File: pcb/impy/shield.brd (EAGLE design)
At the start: 133 x 107 mm, 118 parts, among them J1 USB-2410-06, J2 SI-60062-F, J3 5V, U1 AD5933YRS, U10 LTC3406AB, U11 23LCV1024-I/SN, U12 MIC2009A-1YM6, U13 ADG725BSU, U14 ADG725BSU, U2 ADG704BRM, U3 AD8656ARZ, U4 M24C08WMN, U5 ADG706BRU, U6 DP83848I, U7 MIC2009A-1YM6, U8 AT25DF081A-SS, U9 SST25VF080B-80-4I-S2

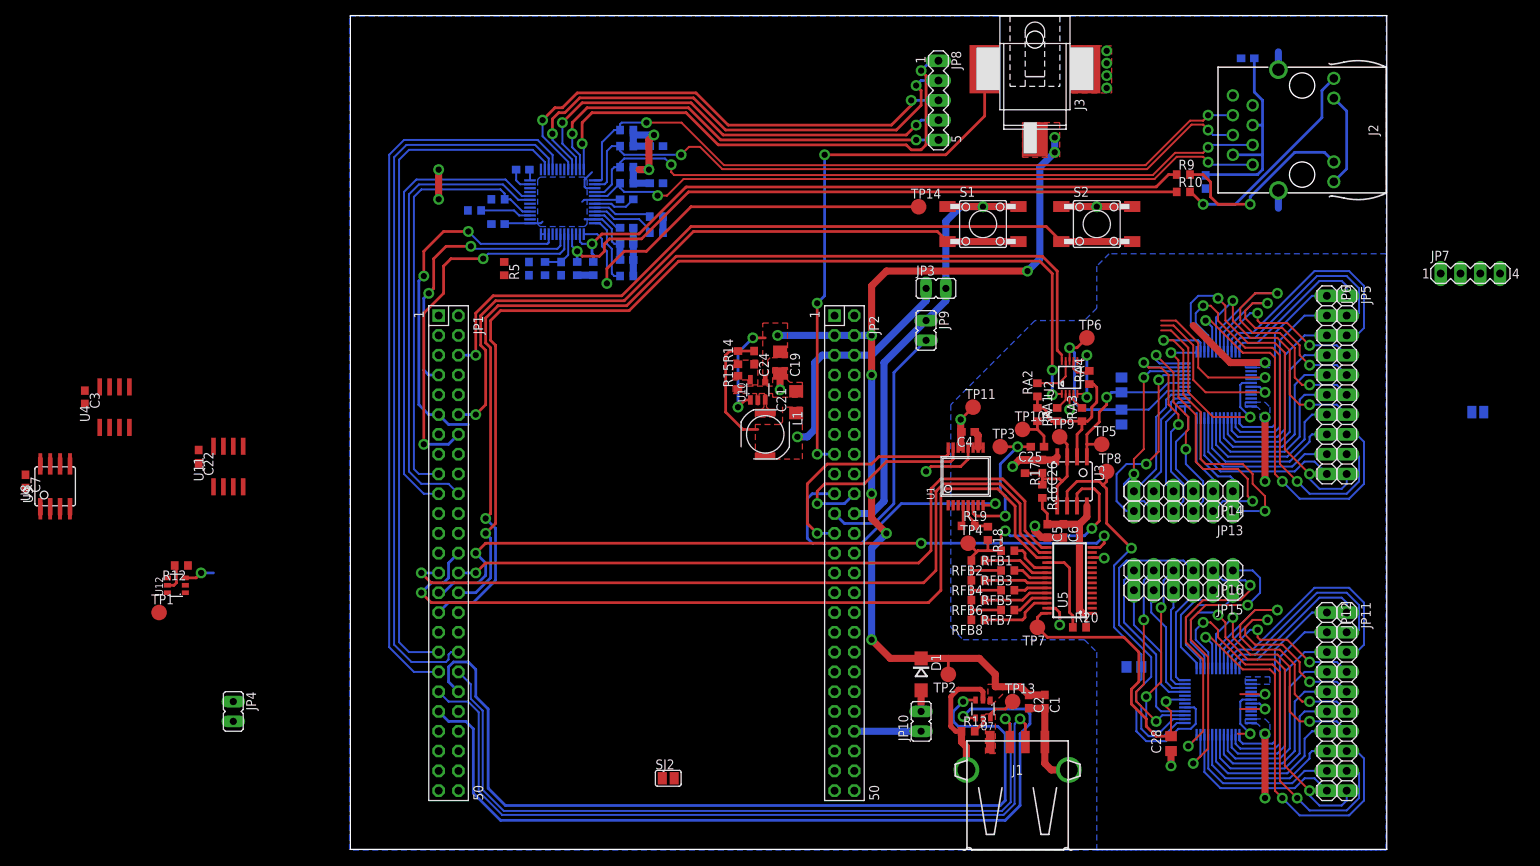
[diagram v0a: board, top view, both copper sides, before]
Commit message: * pcb/impy: (shield.brd) Layout analog circuits and power supply for those.
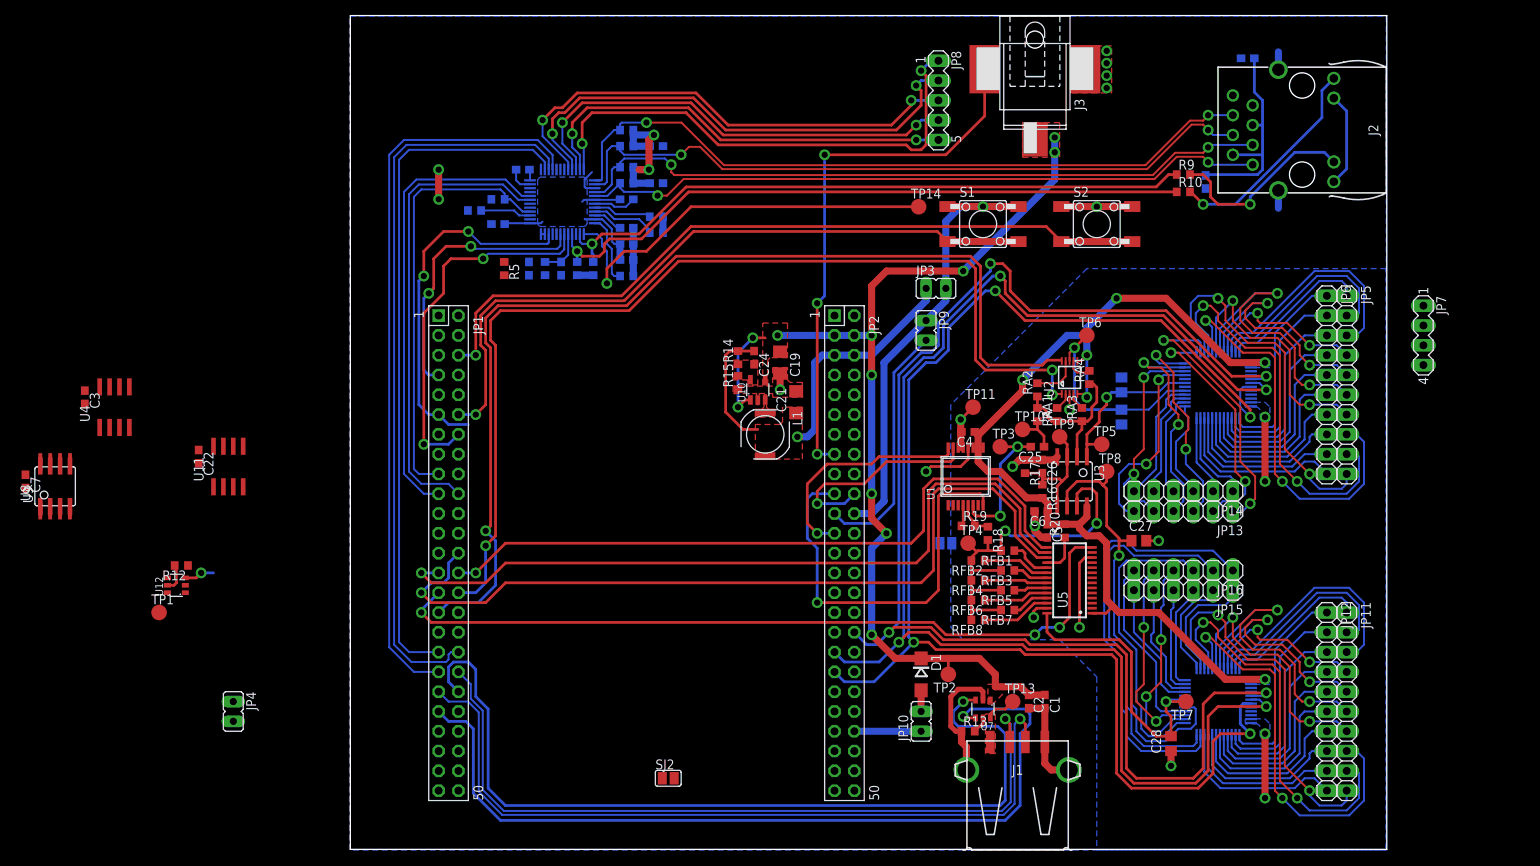
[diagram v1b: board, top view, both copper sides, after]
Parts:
- moved SJ1 70.3 mm to (38.4, 34.3)
- moved TP7 21.3 mm to (69.2, 14.0)
- moved C27 16.2 mm to (63.2, 34.6), flipped to the top
- moved R20 12.5 mm to (53.7, 35.9), turned to 90 degrees
- moved JP7 9.97 mm to (99.7, 61.0), turned to 270 degrees
- moved C6 3.82 mm to (50.6, 38.4), turned to 180 degrees
- moved TP6 0.32 mm to (56.5, 61.0)
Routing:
- net PD2: track 25.1 -> 180.9 mm, vias 2 -> 4
- net PC10: track 26.8 -> 180.1 mm, vias 2 -> 4
- net PC12: track 33.3 -> 181.7 mm, vias 2 -> 4
- net VCC: track 116.6 -> 193.7 mm, vias 5 -> 8
- net PB8: track 37.0 -> 53.0 mm
- net N$96: track 40.3 -> 55.8 mm, vias 2 -> 0
- net N$97: track 36.0 -> 49.8 mm, vias 2 -> 0
- net AGND: track 42.9 -> 52.2 mm, vias 11 -> 12
- net N$107: track 11.0 -> 5.15 mm
- net PE11: track 94.6 -> 100.2 mm
- net N$78: track 41.0 -> 35.5 mm
- net +5V: track 139.8 -> 134.6 mm
- net N$79: track 35.2 -> 31.2 mm
- net PE9: track 100.1 -> 98.3 mm
- net PE10: track 91.0 -> 89.2 mm
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
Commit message: * pcb/impy: (shield.sch) Fix supply of I2C header, should be VDD in case this is supplied from the discovery board or does not match VCC for some other reason.
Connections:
- net VCC: no longer JP7.4
- net VDD: now also JP7.4
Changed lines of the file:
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@@
 <wire x1="35.8775" y1="62.865" x2="30.48" y2="57.4675" width="0.9144" layer="16"/>
 <wire x1="30.48" y1="57.4675" x2="30.48" y2="39.6875" width="0.9144" layer="16"/>
+<contactref element="JP7" pad="4"/>
+<wire x1="47.73" y1="77.4975" x2="99.695" y2="57.15" width="0" layer="19" extent="1-1"/>
 <wire x1="-24.13" y1="60.96" x2="30.48" y2="57.4675" width="0" layer="19" extent="16-16"/>
 <wire x1="-26.67" y1="60.96" x2="-24.13" y2="60.96" width="0" layer="19" extent="1-1"/>
@@
 <contactref element="U11" pad="8"/>
 <contactref element="U11" pad="7"/>
-<contactref element="JP7" pad="4"/>
 <contactref element="J2" pad="2"/>
 <contactref element="J2" pad="5"/>
@@
 <wire x1="79.0575" y1="91.1225" x2="88.2015" y2="91.4019" width="0" layer="19" extent="16-16"/>
 <wire x1="66.675" y1="65.7225" x2="71.755" y2="81.495" width="0" layer="19" extent="1-16"/>
-<wire x1="99.695" y1="57.15" x2="79.375" y2="57.4675" width="0" layer="19" extent="1-1"/>
 <wire x1="2.12" y1="74.13625" x2="42.125" y2="48.5775" width="0" layer="19" extent="1-16"/>
 <wire x1="0.42" y1="80.48625" x2="2.12" y2="76.2" width="0" layer="19" extent="16-16"/>

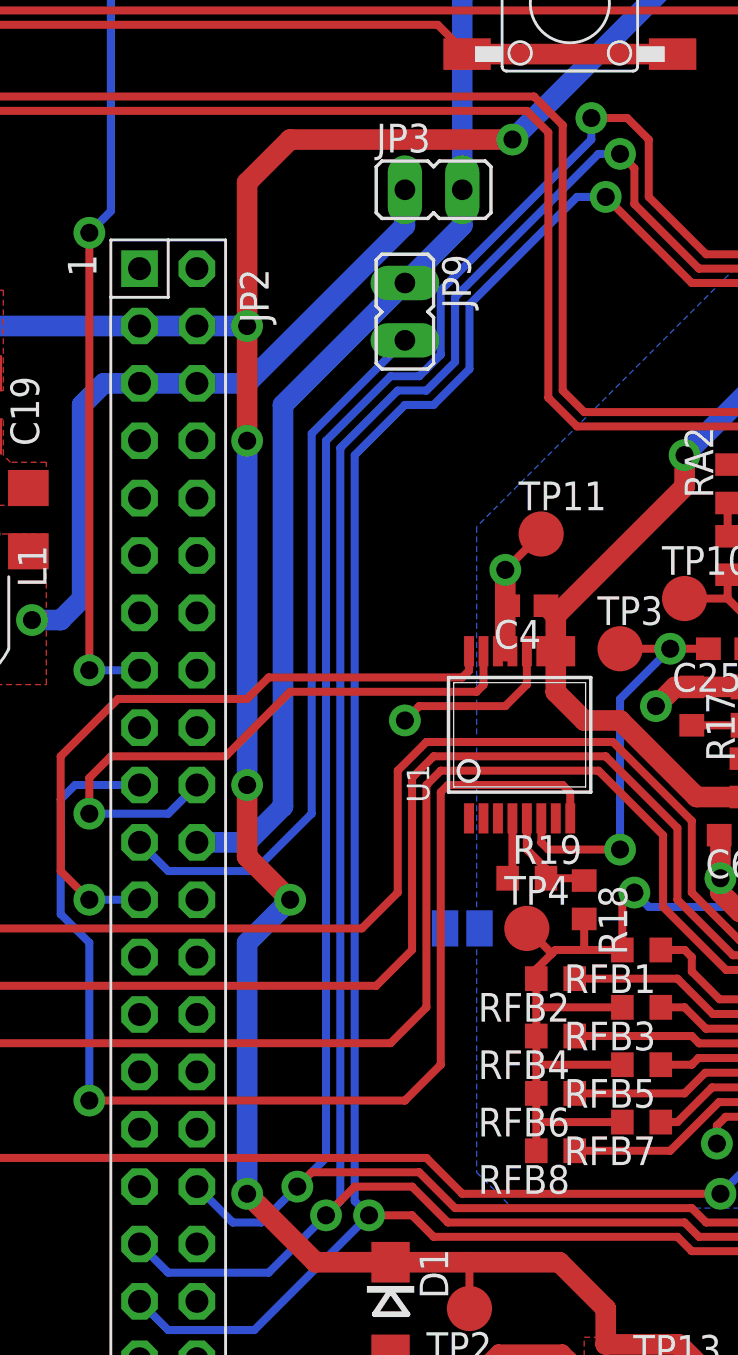
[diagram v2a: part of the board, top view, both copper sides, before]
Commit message: * pcb/impy: (shield.sch) Remove unnecessary BOOT0 jumper, this can be accessed on the discovery board directly.
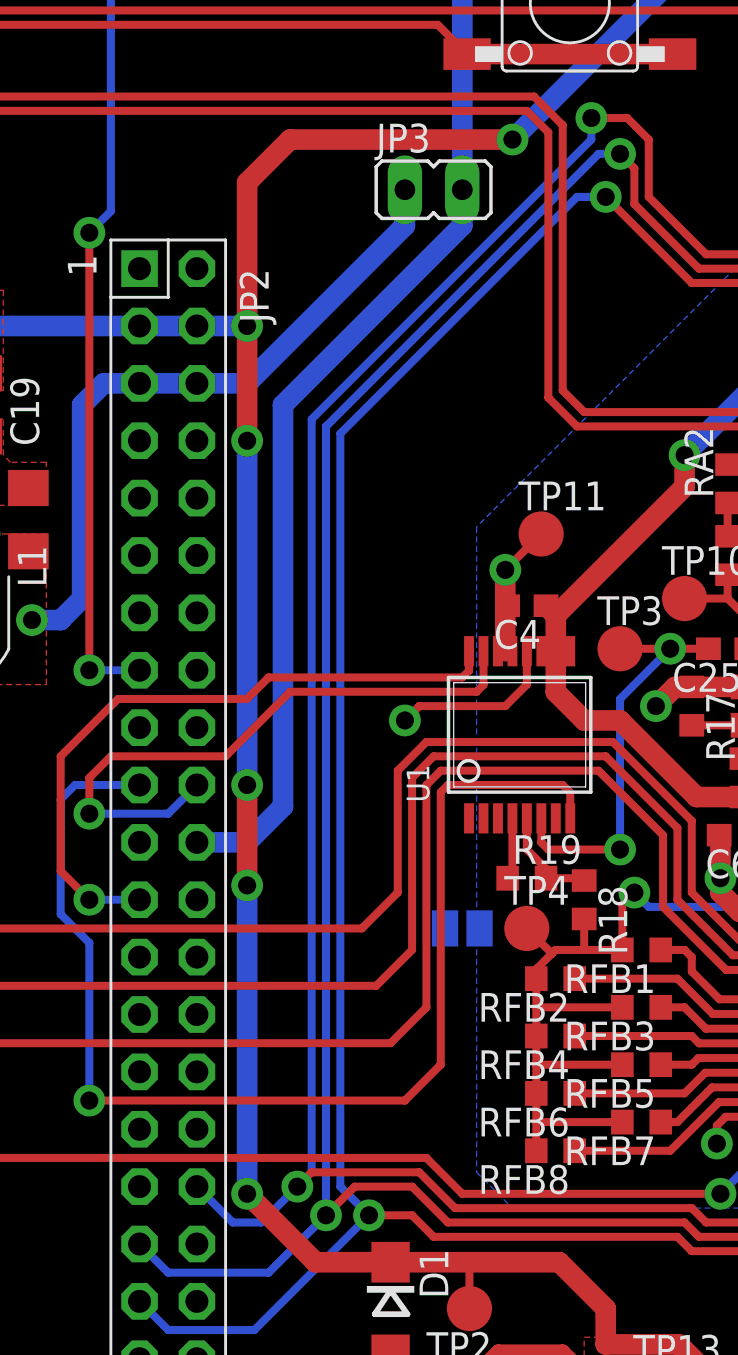
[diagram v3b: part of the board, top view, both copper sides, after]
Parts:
- removed JP9: BOOT0, jumper:JP1
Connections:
- net BOOT0: no longer JP9.2
- net VDD: no longer JP9.1
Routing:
- net BOOT0: track 31.9 -> 0.00 mm
- net +5V: track 134.6 -> 133.0 mm
- net PD2: track 180.9 -> 180.1 mm
- net PC12: track 181.7 -> 180.9 mm
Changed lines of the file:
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@@
 <element name="R11" library="rcl" package="R0603" value="2k2" x="-13.0175" y="69.5325" rot="MR270"/>
 <element name="SJ2" library="jumper" package="SJ" value="ETH_CLK" x="2.794" y="4.1275"/>
-<element name="JP9" library="jumper" package="JP1" value="BOOT0" x="35.8775" y="61.595" rot="R180"/>
 <element name="S2" library="parts" package="FSM" value="FSM4JSMATR" x="57.785" y="75.2475" rot="R270">
 <attribute name="RS" value="718-2455" x="28.575" y="56.1975" size="1.778" layer="27" rot="R270" display="off"/>
@@
 <contactref element="JP1" pad="3"/>
 <contactref element="JP2" pad="22"/>
-<contactref element="JP9" pad="1"/>
 <contactref element="S1" pad="4"/>
 <contactref element="S1" pad="3"/>
@@
 <wire x1="43.1525" y1="77.4975" x2="43.18" y2="77.47" width="0.9144" layer="16"/>
 <wire x1="38.4175" y1="66.9925" x2="38.4175" y2="65.405" width="0.9144" layer="16"/>
-<wire x1="38.4175" y1="65.405" x2="35.8775" y2="62.865" width="0.9144" layer="16"/>
-<wire x1="35.8775" y1="62.865" x2="30.48" y2="57.4675" width="0.9144" layer="16"/>
 <wire x1="30.48" y1="57.4675" x2="30.48" y2="39.6875" width="0.9144" layer="16"/>
 <contactref element="JP7" pad="4"/>
+<wire x1="30.48" y1="57.4675" x2="38.4175" y2="65.405" width="0.9144" layer="16"/>
 <wire x1="47.73" y1="77.4975" x2="99.695" y2="57.15" width="0" layer="19" extent="1-1"/>
 <wire x1="-24.13" y1="60.96" x2="30.48" y2="57.4675" width="0" layer="19" extent="16-16"/>
@@
 <wire x1="28.8925" y1="55.88" x2="28.8925" y2="40.64" width="0.9144" layer="16"/>
 <via x="28.8925" y="40.64" extent="1-16" drill="0.8" shape="octagon"/>
-<via x="30.7975" y="35.56" extent="1-16" drill="0.8" shape="octagon"/>
+<via x="28.8925" y="36.195" extent="1-16" drill="0.8" shape="octagon"/>
 <via x="28.8925" y="22.5425" extent="1-16" drill="0.8" shape="octagon"/>
 <wire x1="28.8925" y1="22.5425" x2="31.9225" y2="19.5125" width="0.9144" layer="1"/>
-<wire x1="28.8925" y1="40.64" x2="28.8925" y2="37.465" width="0.9144" layer="1"/>
-<wire x1="28.8925" y1="37.465" x2="30.7975" y2="35.56" width="0.9144" layer="1"/>
-<wire x1="30.7975" y1="35.56" x2="28.8925" y2="33.655" width="0.9144" layer="16"/>
-<wire x1="28.8925" y1="33.655" x2="28.8925" y2="22.5425" width="0.9144" layer="16"/>
+<wire x1="28.8925" y1="40.64" x2="28.8925" y2="36.195" width="0.9144" layer="1"/>
+<wire x1="28.8925" y1="36.195" x2="28.8925" y2="22.5425" width="0.9144" layer="16"/>
 <via x="40.64" y="69.215" extent="1-16" drill="0.8" shape="octagon"/>
 <wire x1="40.64" y1="69.215" x2="30.7975" y2="69.215" width="0.9144" layer="1"/>
@@
 <signal name="BOOT0">
 <contactref element="JP2" pad="21"/>
-<contactref element="JP9" pad="2"/>
-<wire x1="24.13" y1="38.1" x2="25.4" y2="36.83" width="0.3556" layer="16"/>
-<wire x1="25.4" y1="36.83" x2="29.21" y2="36.83" width="0.3556" layer="16"/>
-<wire x1="29.21" y1="36.83" x2="31.75" y2="39.37" width="0.3556" layer="16"/>
-<wire x1="31.75" y1="39.37" x2="31.75" y2="56.1975" width="0.3556" layer="16"/>
-<wire x1="31.75" y1="56.1975" x2="35.8775" y2="60.325" width="0.3556" layer="16"/>
 </signal>
 <signal name="PE1">
@@
 <wire x1="29.21" y1="16.51" x2="25.4" y2="16.51" width="0.3556" layer="16"/>
 <wire x1="25.4" y1="16.51" x2="24.13" y2="17.78" width="0.3556" layer="16"/>
-<wire x1="33.655" y1="22.225" x2="33.655" y2="55.245" width="0.3556" layer="16"/>
-<wire x1="34.29" y1="21.59" x2="33.655" y2="22.225" width="0.3556" layer="16"/>
-<wire x1="33.655" y1="55.245" x2="35.8775" y2="57.4675" width="0.3556" layer="16"/>
-<wire x1="35.8775" y1="57.4675" x2="37.1475" y2="57.4675" width="0.3556" layer="16"/>
-<wire x1="37.1475" y1="57.4675" x2="38.735" y2="59.055" width="0.3556" layer="16"/>
-<wire x1="38.735" y1="59.055" x2="38.735" y2="61.9125" width="0.3556" layer="16"/>
-<wire x1="38.735" y1="61.9125" x2="43.4975" y2="66.675" width="0.3556" layer="16"/>
+<wire x1="33.02" y1="22.86" x2="33.02" y2="56.1975" width="0.3556" layer="16"/>
+<wire x1="34.29" y1="21.59" x2="33.02" y2="22.86" width="0.3556" layer="16"/>
+<wire x1="33.02" y1="56.1975" x2="43.4975" y2="66.675" width="0.3556" layer="16"/>
 <wire x1="77.5925" y1="54.36" x2="76.585" y2="54.36" width="0.254" layer="16"/>
 <wire x1="76.585" y1="54.36" x2="76.2" y2="53.975" width="0.254" layer="16"/>
@@
 <wire x1="29.845" y1="19.05" x2="25.4" y2="19.05" width="0.3556" layer="16"/>
 <wire x1="25.4" y1="19.05" x2="24.13" y2="20.32" width="0.3556" layer="16"/>
-<wire x1="32.385" y1="21.59" x2="33.02" y2="22.225" width="0.3556" layer="16"/>
-<wire x1="33.02" y1="22.225" x2="33.02" y2="55.5625" width="0.3556" layer="16"/>
-<wire x1="33.02" y1="55.5625" x2="35.56" y2="58.1025" width="0.3556" layer="16"/>
-<wire x1="35.56" y1="58.1025" x2="36.83" y2="58.1025" width="0.3556" layer="16"/>
-<wire x1="36.83" y1="58.1025" x2="38.1" y2="59.3725" width="0.3556" layer="16"/>
-<wire x1="38.1" y1="59.3725" x2="38.1" y2="62.23" width="0.3556" layer="16"/>
-<wire x1="38.1" y1="62.23" x2="44.45" y2="68.58" width="0.3556" layer="16"/>
+<wire x1="32.385" y1="56.515" x2="44.45" y2="68.58" width="0.3556" layer="16"/>
 <wire x1="44.45" y1="68.58" x2="45.4025" y2="68.58" width="0.3556" layer="16"/>
 <via x="45.4025" y="68.58" extent="1-16" drill="0.8" shape="octagon"/>
@@
 <wire x1="46.0375" y1="66.3575" x2="46.0375" y2="67.945" width="0.3556" layer="1"/>
 <wire x1="46.0375" y1="67.945" x2="45.4025" y2="68.58" width="0.3556" layer="1"/>
+<wire x1="32.385" y1="56.515" x2="32.385" y2="21.59" width="0.3556" layer="16"/>
 <wire x1="-51.7525" y1="46.7325" x2="24.13" y2="20.32" width="0" layer="19" extent="1-1"/>
 <wire x1="-73.9775" y1="44.7465" x2="-51.7525" y2="46.7325" width="0" layer="19" extent="1-1"/>
@@
 <wire x1="29.5275" y1="21.2725" x2="28.2575" y2="21.2725" width="0.3556" layer="16"/>
 <wire x1="28.2575" y1="21.2725" x2="26.67" y2="22.86" width="0.3556" layer="16"/>
-<wire x1="31.115" y1="22.86" x2="32.385" y2="24.13" width="0.3556" layer="16"/>
-<wire x1="32.385" y1="24.13" x2="32.385" y2="55.88" width="0.3556" layer="16"/>
-<wire x1="32.385" y1="55.88" x2="35.2425" y2="58.7375" width="0.3556" layer="16"/>
-<wire x1="35.2425" y1="58.7375" x2="36.5125" y2="58.7375" width="0.3556" layer="16"/>
-<wire x1="36.5125" y1="58.7375" x2="37.465" y2="59.69" width="0.3556" layer="16"/>
-<wire x1="37.465" y1="59.69" x2="37.465" y2="62.5475" width="0.3556" layer="16"/>
-<wire x1="37.465" y1="62.5475" x2="44.1325" y2="69.215" width="0.3556" layer="16"/>
+<wire x1="31.115" y1="22.86" x2="31.75" y2="23.495" width="0.3556" layer="16"/>
+<wire x1="31.75" y1="23.495" x2="31.75" y2="56.8325" width="0.3556" layer="16"/>
+<wire x1="31.75" y1="56.8325" x2="44.1325" y2="69.215" width="0.3556" layer="16"/>
 <wire x1="44.1325" y1="69.215" x2="44.1325" y2="70.1675" width="0.3556" layer="16"/>
 <via x="44.1325" y="70.1675" extent="1-16" drill="0.8" shape="octagon"/>
